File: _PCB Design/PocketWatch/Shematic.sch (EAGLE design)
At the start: 28 parts, among them Q1 MMBTA56-SOT23, U2 ATTINY88-AU

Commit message: Sync Changes
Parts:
- added R5, R6, R7, R8: 30, eagle-ltspice:RR1206
- added SV6: (no value), con-lstb:MA06-1
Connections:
- new net N$1: R8.2, T4.B
- new net N$2: R7.2, T3.B
- new net N$3: R6.2, T2.B
- new net N$5: R5.2, T1.B
- net EN0: now also R5.1; no longer T1.B
- net EN1: now also R6.1; no longer T2.B
- net EN2: now also R7.1; no longer T3.B
- net EN3: now also R8.1; no longer T4.B
- net GND: now also SV6.1
- net MISO: now also SV6.5
- net MOSI: now also SV6.6
- net RESET: now also SV6.3
- net SCK: now also SV6.4
- net VCC: now also SV6.2
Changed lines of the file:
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@@
 <part name="SV2" library="con-lstb" library_urn="urn:adsk.eagle:library:162" deviceset="MA08-1" device="" package3d_urn="urn:adsk.eagle:package:8343/1"/>
 <part name="SV5" library="con-lstb" library_urn="urn:adsk.eagle:library:162" deviceset="MA04-1" device="" package3d_urn="urn:adsk.eagle:package:8337/1"/>
+<part name="SV6" library="con-lstb" library_urn="urn:adsk.eagle:library:162" deviceset="MA06-1" device="" package3d_urn="urn:adsk.eagle:package:8340/1"/>
+<part name="R5" library="eagle-ltspice" library_urn="urn:adsk.eagle:library:217" deviceset="R" device="R1206" package3d_urn="urn:adsk.eagle:package:13301/1" value="30"/>
+<part name="R6" library="eagle-ltspice" library_urn="urn:adsk.eagle:library:217" deviceset="R" device="R1206" package3d_urn="urn:adsk.eagle:package:13301/1" value="30"/>
+<part name="R7" library="eagle-ltspice" library_urn="urn:adsk.eagle:library:217" deviceset="R" device="R1206" package3d_urn="urn:adsk.eagle:package:13301/1" value="30"/>
+<part name="R8" library="eagle-ltspice" library_urn="urn:adsk.eagle:library:217" deviceset="R" device="R1206" package3d_urn="urn:adsk.eagle:package:13301/1" value="30"/>
 </parts>
 <sheets>
@@
 <instance part="SV2" gate="1" x="165.1" y="53.34" rot="R180"/>
 <instance part="SV5" gate="1" x="162.56" y="0"/>
+<instance part="SV6" gate="1" x="-53.34" y="-7.62"/>
+<instance part="R5" gate="G$1" x="200.66" y="-12.7" rot="R90"/>
+<instance part="R6" gate="G$1" x="233.68" y="-12.7" rot="R90"/>
+<instance part="R7" gate="G$1" x="266.7" y="-12.7" rot="R90"/>
+<instance part="R8" gate="G$1" x="299.72" y="-12.7" rot="R90"/>
 </instances>
 <busses>
@@
 <label x="17.78" y="-12.7" size="1.778" layer="95"/>
 </segment>
+<segment>
+<pinref part="SV6" gate="1" pin="5"/>
+<wire x1="-45.72" y1="-5.08" x2="-33.02" y2="-5.08" width="0.1524" layer="91"/>
+<label x="-43.18" y="-5.08" size="1.778" layer="95"/>
+</segment>
 </net>
 <net name="RESET" class="0">
@@
 <wire x1="101.6" y1="-20.32" x2="114.3" y2="-20.32" width="0.1524" layer="91"/>
 <label x="104.14" y="-20.32" size="1.778" layer="95"/>
+</segment>
+<segment>
+<pinref part="SV6" gate="1" pin="3"/>
+<wire x1="-45.72" y1="-10.16" x2="-33.02" y2="-10.16" width="0.1524" layer="91"/>
+<label x="-43.18" y="-10.16" size="1.778" layer="95"/>
 </segment>
 </net>
@@
 <wire x1="307.34" y1="-10.16" x2="317.5" y2="-10.16" width="0.1524" layer="91"/>
 <label x="309.88" y="-10.16" size="1.778" layer="95"/>
+</segment>
+<segment>
+<pinref part="SV6" gate="1" pin="1"/>
+<wire x1="-45.72" y1="-15.24" x2="-33.02" y2="-15.24" width="0.1524" layer="91"/>
+<label x="-43.18" y="-15.24" size="1.778" layer="95"/>
 </segment>
 </net>
@@
 <junction x="-25.4" y="53.34"/>
 </segment>
+<segment>
+<pinref part="SV6" gate="1" pin="2"/>
+<wire x1="-45.72" y1="-12.7" x2="-33.02" y2="-12.7" width="0.1524" layer="91"/>
+<label x="-43.18" y="-12.7" size="1.778" layer="95"/>
+</segment>
 </net>
 <net name="MOSI" class="0">
@@
 <label x="17.78" y="-10.16" size="1.778" layer="95"/>
 </segment>
+<segment>
+<pinref part="SV6" gate="1" pin="6"/>
+<wire x1="-45.72" y1="-2.54" x2="-33.02" y2="-2.54" width="0.1524" layer="91"/>
+<label x="-43.18" y="-2.54" size="1.778" layer="95"/>
+</segment>
 </net>
 <net name="SCK" class="0">
@@
 <wire x1="27.94" y1="-15.24" x2="15.24" y2="-15.24" width="0.1524" layer="91"/>
 <label x="17.78" y="-15.24" size="1.778" layer="95"/>
+</segment>
+<segment>
+<pinref part="SV6" gate="1" pin="4"/>
+<wire x1="-45.72" y1="-7.62" x2="-33.02" y2="-7.62" width="0.1524" layer="91"/>
+<label x="-43.18" y="-7.62" size="1.778" layer="95"/>
 </segment>
 </net>
@@
 </segment>
 <segment>
-<pinref part="T1" gate="G$1" pin="B"/>
-<wire x1="203.2" y1="-5.08" x2="193.04" y2="-5.08" width="0.1524" layer="91"/>
-<label x="195.58" y="-5.08" size="1.778" layer="95"/>
+<pinref part="R5" gate="G$1" pin="1"/>
+<wire x1="200.66" y1="-17.78" x2="200.66" y2="-20.32" width="0.1524" layer="91"/>
+<wire x1="200.66" y1="-20.32" x2="190.5" y2="-20.32" width="0.1524" layer="91"/>
+<label x="193.04" y="-20.32" size="1.778" layer="95"/>
 </segment>
 </net>
@@
 </segment>
 <segment>
-<pinref part="T2" gate="G$1" pin="B"/>
-<wire x1="236.22" y1="-5.08" x2="226.06" y2="-5.08" width="0.1524" layer="91"/>
-<label x="228.6" y="-5.08" size="1.778" layer="95"/>
+<pinref part="R6" gate="G$1" pin="1"/>
+<wire x1="233.68" y1="-17.78" x2="233.68" y2="-20.32" width="0.1524" layer="91"/>
+<wire x1="233.68" y1="-20.32" x2="223.52" y2="-20.32" width="0.1524" layer="91"/>
+<label x="226.06" y="-20.32" size="1.778" layer="95"/>
 </segment>
 </net>
@@
 </segment>
 <segment>
-<pinref part="T3" gate="G$1" pin="B"/>
-<wire x1="269.24" y1="-5.08" x2="259.08" y2="-5.08" width="0.1524" layer="91"/>
-<label x="261.62" y="-5.08" size="1.778" layer="95"/>
+<pinref part="R7" gate="G$1" pin="1"/>
+<wire x1="266.7" y1="-17.78" x2="266.7" y2="-20.32" width="0.1524" layer="91"/>
+<wire x1="266.7" y1="-20.32" x2="256.54" y2="-20.32" width="0.1524" layer="91"/>
+<label x="259.08" y="-20.32" size="1.778" layer="95"/>
 </segment>
 </net>
@@
 </segment>
 <segment>
-<pinref part="T4" gate="G$1" pin="B"/>
-<wire x1="302.26" y1="-5.08" x2="292.1" y2="-5.08" width="0.1524" layer="91"/>
-<label x="294.64" y="-5.08" size="1.778" layer="95"/>
+<pinref part="R8" gate="G$1" pin="1"/>
+<wire x1="299.72" y1="-17.78" x2="299.72" y2="-20.32" width="0.1524" layer="91"/>
+<wire x1="299.72" y1="-20.32" x2="289.56" y2="-20.32" width="0.1524" layer="91"/>
+<label x="292.1" y="-20.32" size="1.778" layer="95"/>
 </segment>
 </net>
@@
 </segment>
 </net>
+<net name="N$1" class="0">
+<segment>
+<pinref part="T4" gate="G$1" pin="B"/>
+<wire x1="302.26" y1="-5.08" x2="299.72" y2="-5.08" width="0.1524" layer="91"/>
+<pinref part="R8" gate="G$1" pin="2"/>
+<wire x1="299.72" y1="-5.08" x2="299.72" y2="-7.62" width="0.1524" layer="91"/>
+</segment>
+</net>
+<net name="N$2" class="0">
+<segment>
+<pinref part="T3" gate="G$1" pin="B"/>
+<pinref part="R7" gate="G$1" pin="2"/>
+<wire x1="269.24" y1="-5.08" x2="266.7" y2="-5.08" width="0.1524" layer="91"/>
+<wire x1="266.7" y1="-5.08" x2="266.7" y2="-7.62" width="0.1524" layer="91"/>
+</segment>
+</net>
+<net name="N$3" class="0">
+<segment>
+<pinref part="T2" gate="G$1" pin="B"/>
+<pinref part="R6" gate="G$1" pin="2"/>
+<wire x1="236.22" y1="-5.08" x2="233.68" y2="-5.08" width="0.1524" layer="91"/>
+<wire x1="233.68" y1="-5.08" x2="233.68" y2="-7.62" width="0.1524" layer="91"/>
+</segment>
+</net>
+<net name="N$5" class="0">
+<segment>
+<pinref part="T1" gate="G$1" pin="B"/>
+<pinref part="R5" gate="G$1" pin="2"/>
+<wire x1="203.2" y1="-5.08" x2="200.66" y2="-5.08" width="0.1524" layer="91"/>
+<wire x1="200.66" y1="-5.08" x2="200.66" y2="-7.62" width="0.1524" layer="91"/>
+</segment>
+</net>

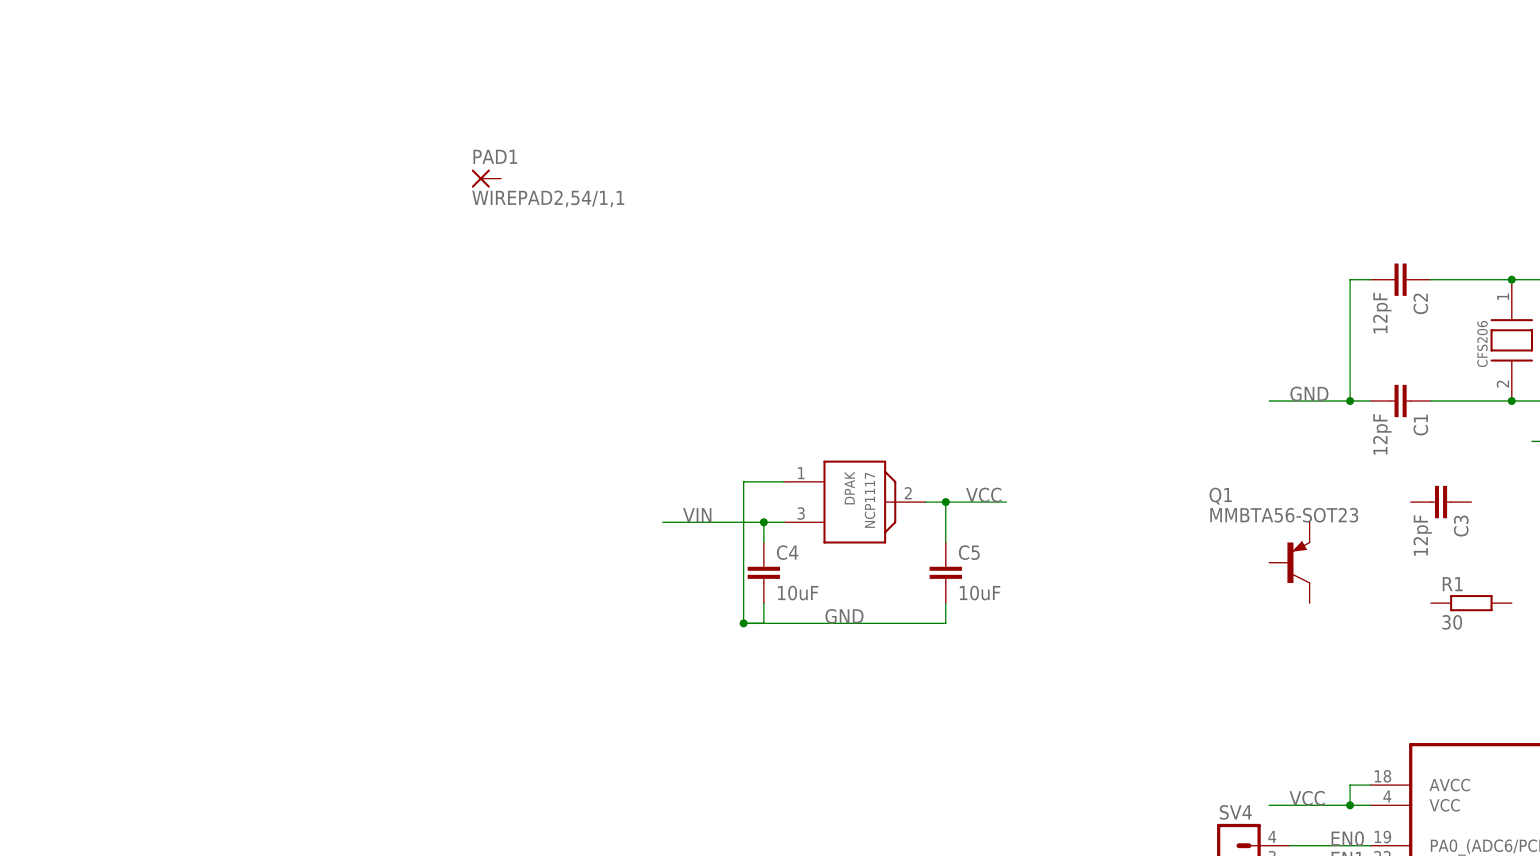
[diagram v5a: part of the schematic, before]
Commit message: Added Boost circuitry
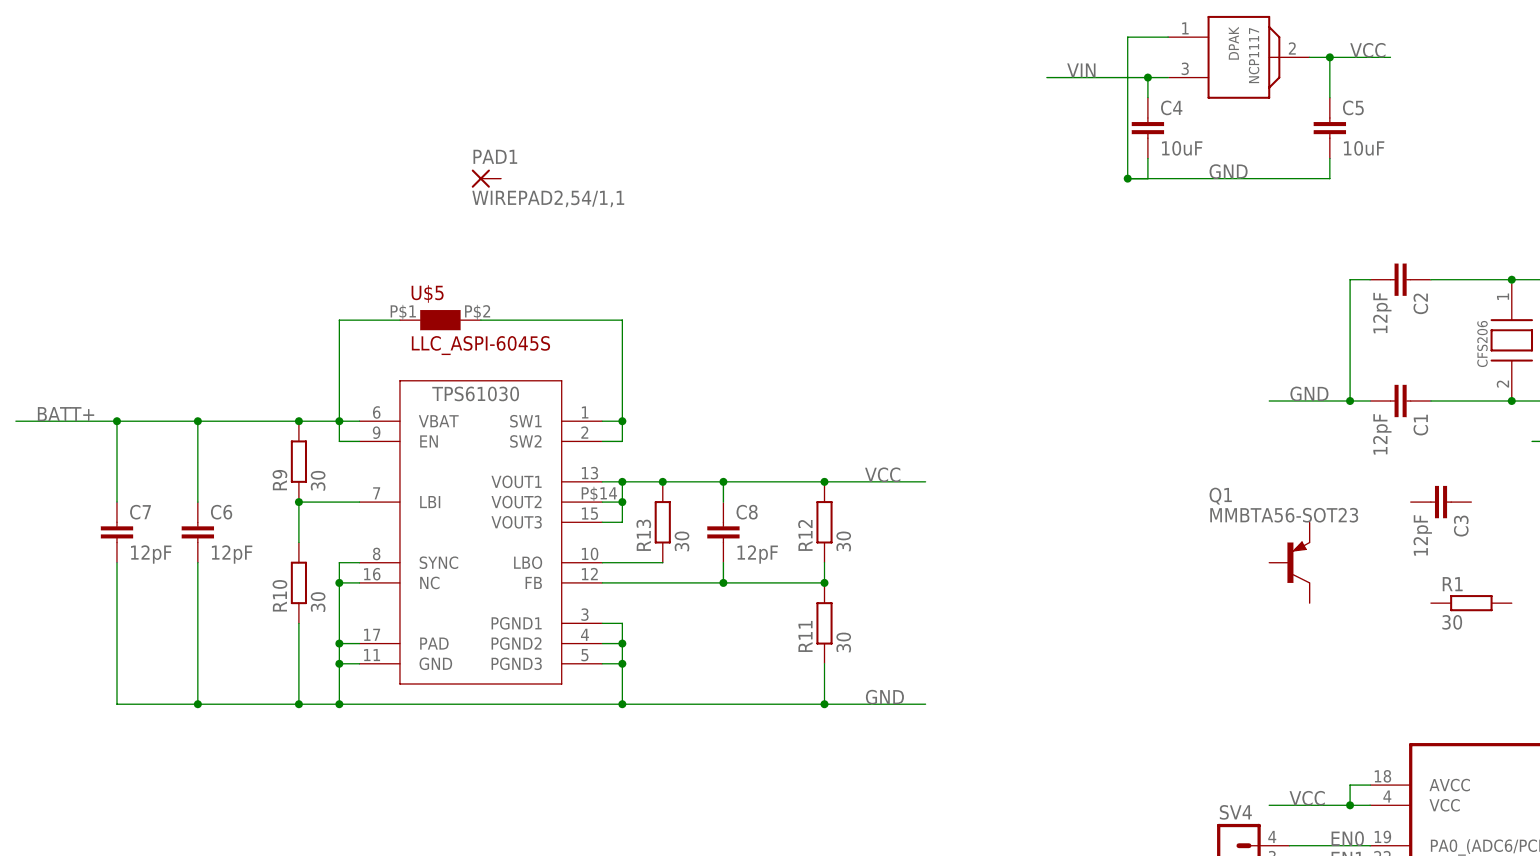
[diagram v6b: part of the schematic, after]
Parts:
- added C6, C7, C8: 12pF, eagle-ltspice:CC1206
- added R10, R11, R12, R13, R9: 30, eagle-ltspice:RR1206
- added U$5: LLC_ASPI-6045S, Library:LLC_ASPI-6045S
- added U$6: TPS61030, Library:TPS61030
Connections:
- new net BATT+: C6.1, C7.1, R9.2, U$5.P$1, U$6.EN, U$6.VBAT
- new net N$10: R13.1, U$6.LBO
- new net N$11: R10.2, R9.1, U$6.LBI
- new net N$13: C8.2, R11.2, R12.1, U$6.FB
- new net N$8: U$5.P$2, U$6.SW1, U$6.SW2
- net GND: now also C6.2, C7.2, R10.1, R11.1, U$6.GND, U$6.NC, U$6.PAD, U$6.PGND1, U$6.PGND2, U$6.PGND3, U$6.SYNC
- net VCC: now also C8.1, R12.2, R13.2, U$6.VOUT1, U$6.VOUT2, U$6.VOUT3
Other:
- moved on the sheet: C4, C5, NCP1117
